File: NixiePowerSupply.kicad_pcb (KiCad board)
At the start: 2 copper layers, 57.2 x 40.6 mm, 26 parts, among them J1 BARREL_JACK, P1 CONN_01X03, P2 CONN_01X03, T1 IRF644, U1 MAX1771

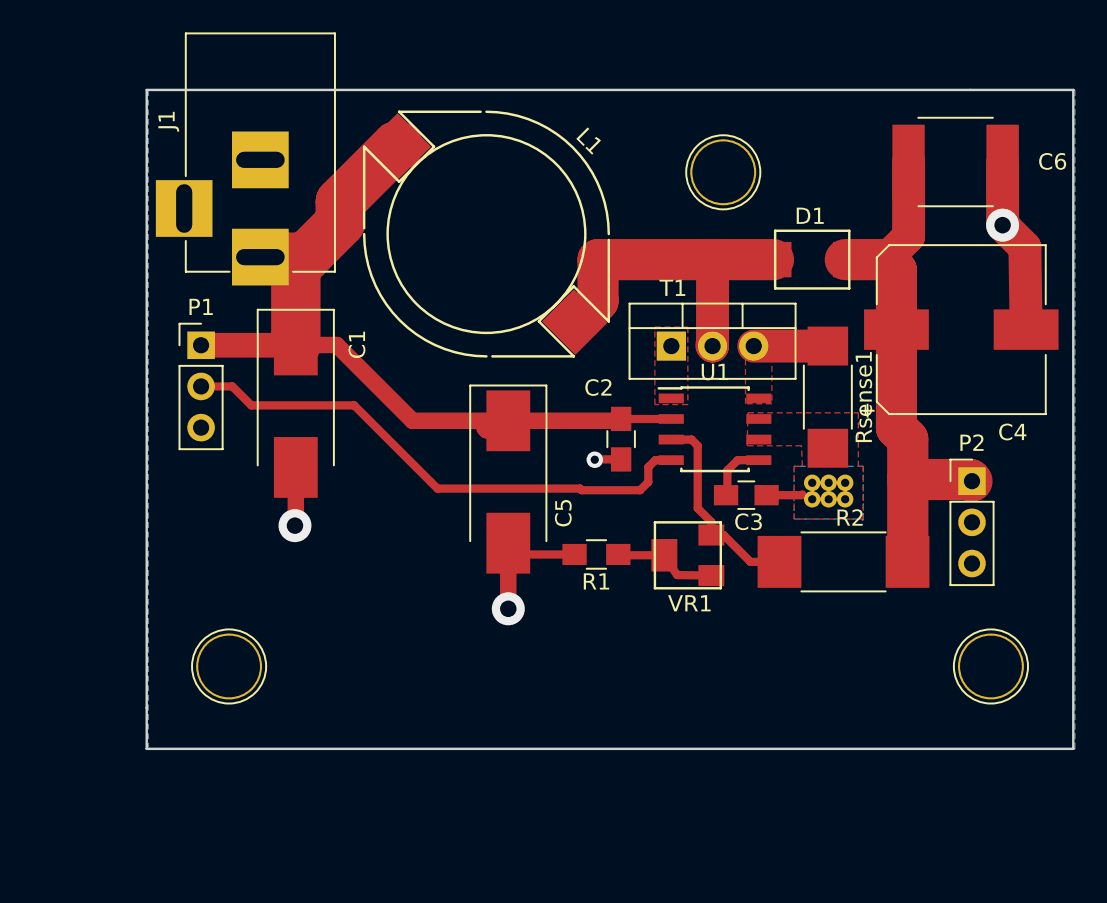
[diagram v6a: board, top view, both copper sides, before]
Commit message: Fixed output connector
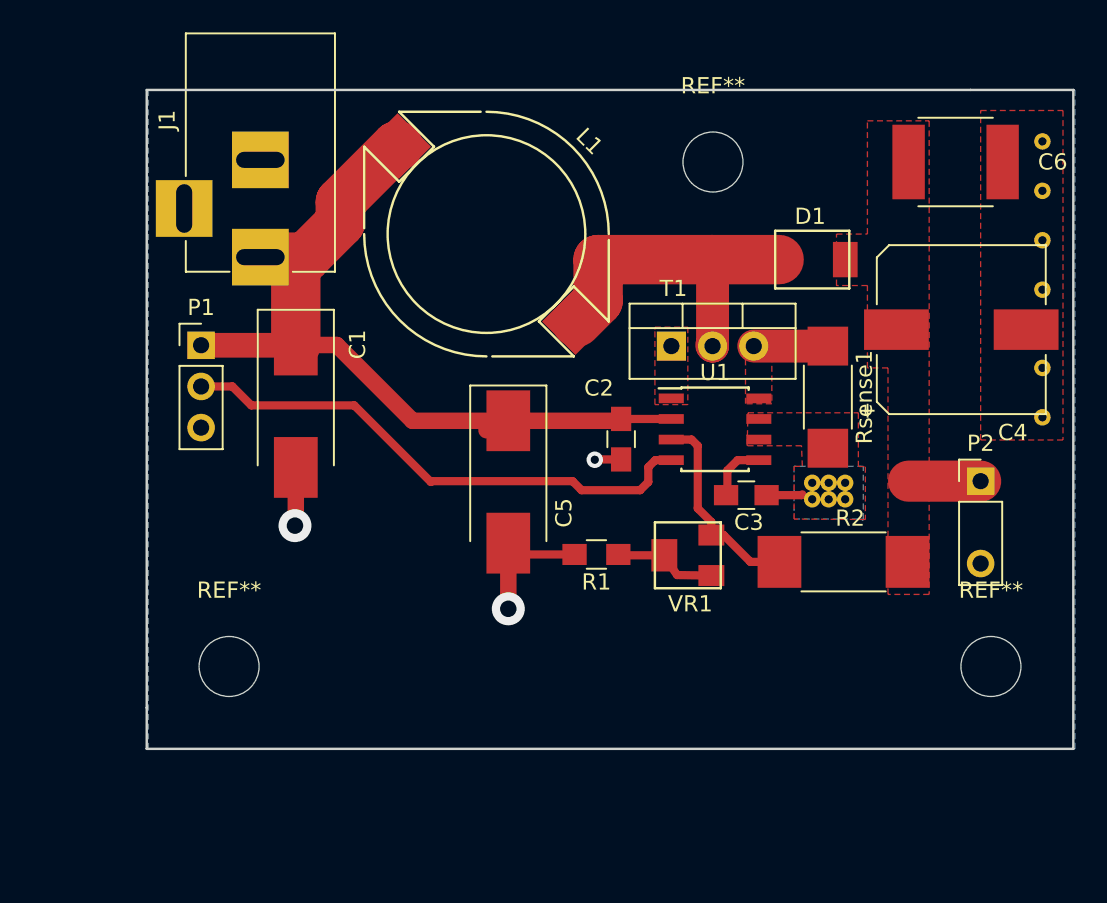
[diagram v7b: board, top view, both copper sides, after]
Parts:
- removed the REF** at (160.0, 80.0)
- removed the REF** at (129.5, 110.5)
- removed the REF** at (176.5, 110.5)
- added REF**: MountingHole_3.7mm, Mounting_Holes:MountingHole_3.7mm, F.Cu at (159.4, 79.4)
- added REF**: Via, nixie:Via, F.Cu at (179.7, 92.1)
- added REF**: MountingHole_3.7mm, Mounting_Holes:MountingHole_3.7mm, F.Cu at (129.5, 110.5)
- added REF**: MountingHole_3.7mm, Mounting_Holes:MountingHole_3.7mm, F.Cu at (176.5, 110.5)
- added REF**: Via, nixie:Via, F.Cu at (179.7, 95.1)
- added REF**: Via, nixie:Via, F.Cu at (179.7, 87.2)
- added REF**: Via, nixie:Via, F.Cu at (179.7, 84.2)
- added REF**: Via, nixie:Via, F.Cu at (179.7, 81.2)
- added REF**: Via, nixie:Via, F.Cu at (179.7, 78.1)
- P2: footprint Pin_Headers:Pin_Header_Straight_1x03_Pitch2.54mm -> nixie:Pin_Header_Straight_1x03_Pitch2.54mm_No_Center
- moved P2 0.53 mm to (175.9, 99.1)
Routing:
- net Net-(C4-Pad1): track 33.1 -> 5.21 mm
- net GND: track 27.1 -> 16.0 mm, vias 4 -> 3
- added copper zone on F.Cu, net Net-(C4-Pad1)

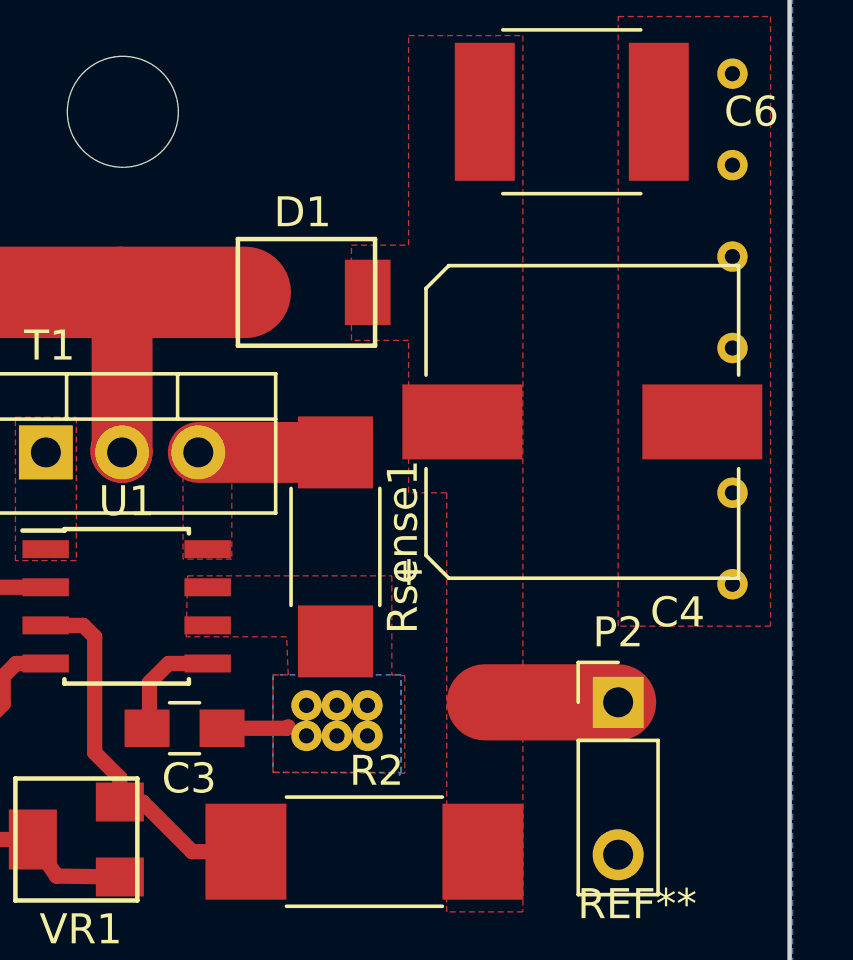
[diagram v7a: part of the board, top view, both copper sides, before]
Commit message: More fiddling with via stitching
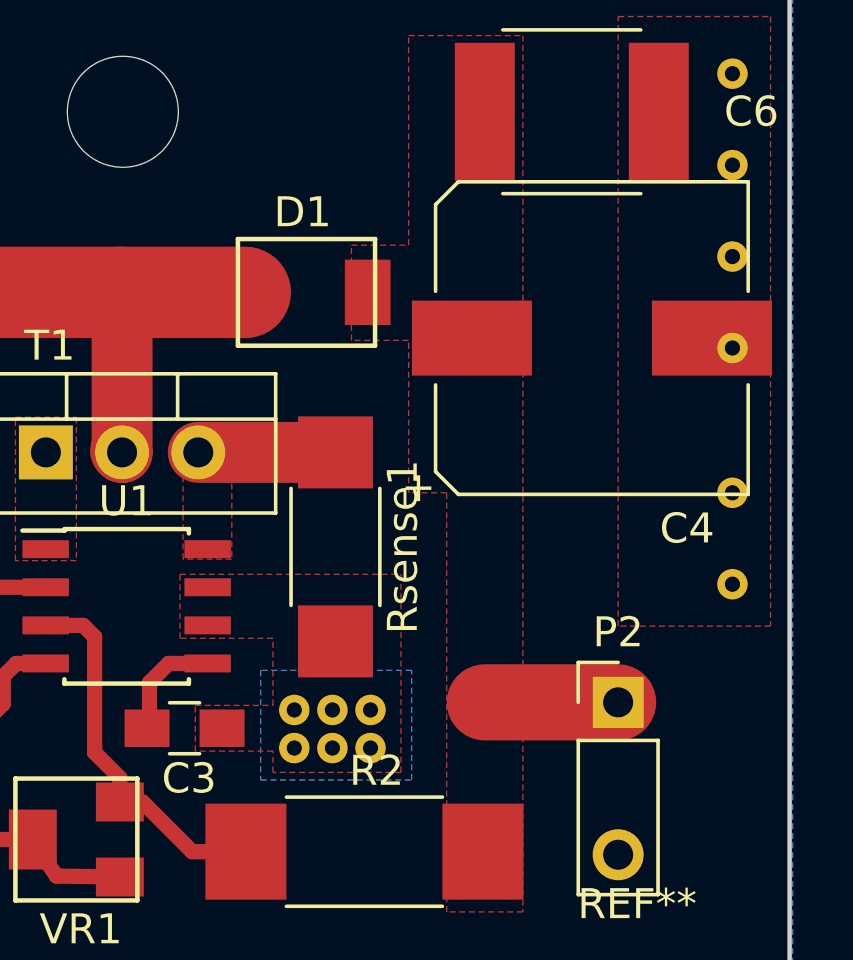
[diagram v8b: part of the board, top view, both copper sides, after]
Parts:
- removed the REF** at (165.5, 100.2)
- removed the REF** at (167.5, 99.2)
- removed the REF** at (166.5, 99.2)
- removed the REF** at (165.5, 99.2)
- removed the REF** at (167.5, 100.2)
- removed the REF** at (166.5, 100.2)
- added REF**: Via, nixie:Via, F.Cu at (167.6, 100.6)
- added REF**: Via, nixie:Via, F.Cu at (165.1, 99.3)
- added REF**: Via, nixie:Via, F.Cu at (166.4, 100.6)
- added REF**: Via, nixie:Via, F.Cu at (165.1, 100.6)
- added REF**: Via, nixie:Via, F.Cu at (167.6, 99.3)
- added REF**: Via, nixie:Via, F.Cu at (166.4, 99.3)
- moved C4 2.81 mm to (175.0, 86.9)
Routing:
- net GND: track 16.0 -> 13.7 mm
- net Net-(C4-Pad1): track 5.21 -> 4.46 mm
